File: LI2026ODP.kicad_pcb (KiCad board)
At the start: 4 copper layers, 18.8 x 39.9 mm, 34 parts, among them J1 9-1437539-2, J2 Conn_01x05_Male, U1 LM2936MM-3.3, U2 STM32G0B1KET6, U3 max6921aui

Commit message: Added SWCLK silk to PCB.
 Add SWCLK silk
 Issue : #6

 This was missing in the original design.
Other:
- board text added: "SWCLK"
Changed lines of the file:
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@@
   (general
     (thickness 1.6)
-    (drawings 12)
+    (drawings 13)
     (tracks 335)
     (zones 0)
@@
   (page A4)
   (layers
-    (0 F.Cu signal hide)
-    (1 In1.Cu power hide)
-    (2 In2.Cu signal hide)
-    (31 B.Cu signal hide)
+    (0 F.Cu signal)
+    (1 In1.Cu power)
+    (2 In2.Cu signal)
+    (31 B.Cu signal)
     (32 B.Adhes user hide)
     (33 F.Adhes user hide)
-    (34 B.Paste user hide)
+    (34 B.Paste user)
     (35 F.Paste user hide)
     (36 B.SilkS user)
-    (37 F.SilkS user hide)
+    (37 F.SilkS user)
     (38 B.Mask user)
-    (39 F.Mask user hide)
+    (39 F.Mask user)
     (40 Dwgs.User user hide)
     (41 Cmts.User user hide)
@@
       (net 76 /KEY0))
   )
+  (gr_text SWCLK (at 119.888 120.142) (layer F.SilkS)
+    (effects (font (size 0.6 0.5) (thickness 0.1)))
+  )
   (gr_text v1.0.0 (at 120.65 92.456 270) (layer F.SilkS)

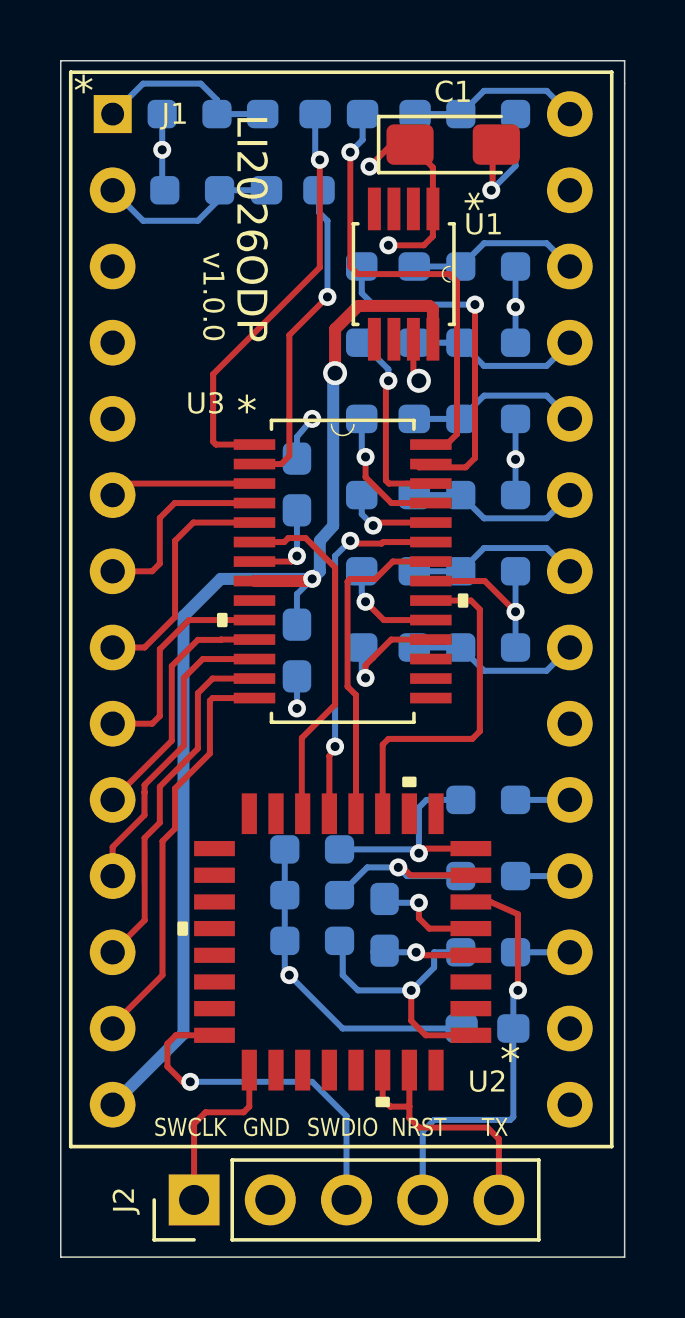
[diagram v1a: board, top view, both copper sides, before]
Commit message: Modify the U2 Footprint.
 Issue : #5

 The footprint was incorrect. Substitute it with the right 0.8mm pitch one.
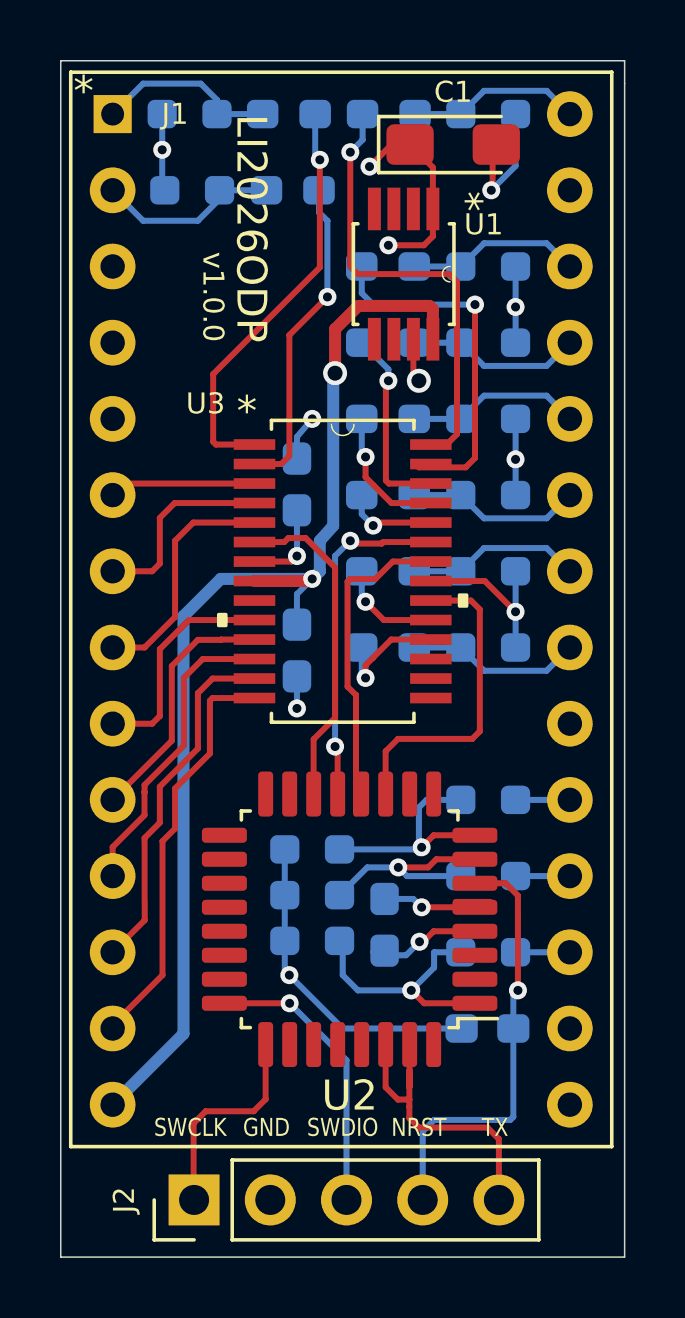
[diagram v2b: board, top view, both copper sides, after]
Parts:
- U2: footprint STM32G0B1:STM32G0B1KET6 -> Package_QFP:LQFP-32_7x7mm_P0.8mm
- moved U2 0.79 mm to (125.2, 113.2)
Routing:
- net /SWDIO: track 11.9 -> 9.34 mm
- net /LPUART2_TX: track 8.86 -> 10.7 mm
- net /SWCLK: track 6.47 -> 7.59 mm
- net /MOSI: track 12.6 -> 11.5 mm
- net /KEY0: track 9.21 -> 8.31 mm
- net /BLANK: track 11.5 -> 10.7 mm
- net GND: track 36.6 -> 37.3 mm
- net /LOAD: track 12.1 -> 11.4 mm
- net /KEY2: track 7.01 -> 7.67 mm

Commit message: Add capacitor for 25v line
 Issue #8 .

 Add C6 close to the voltage regulator.
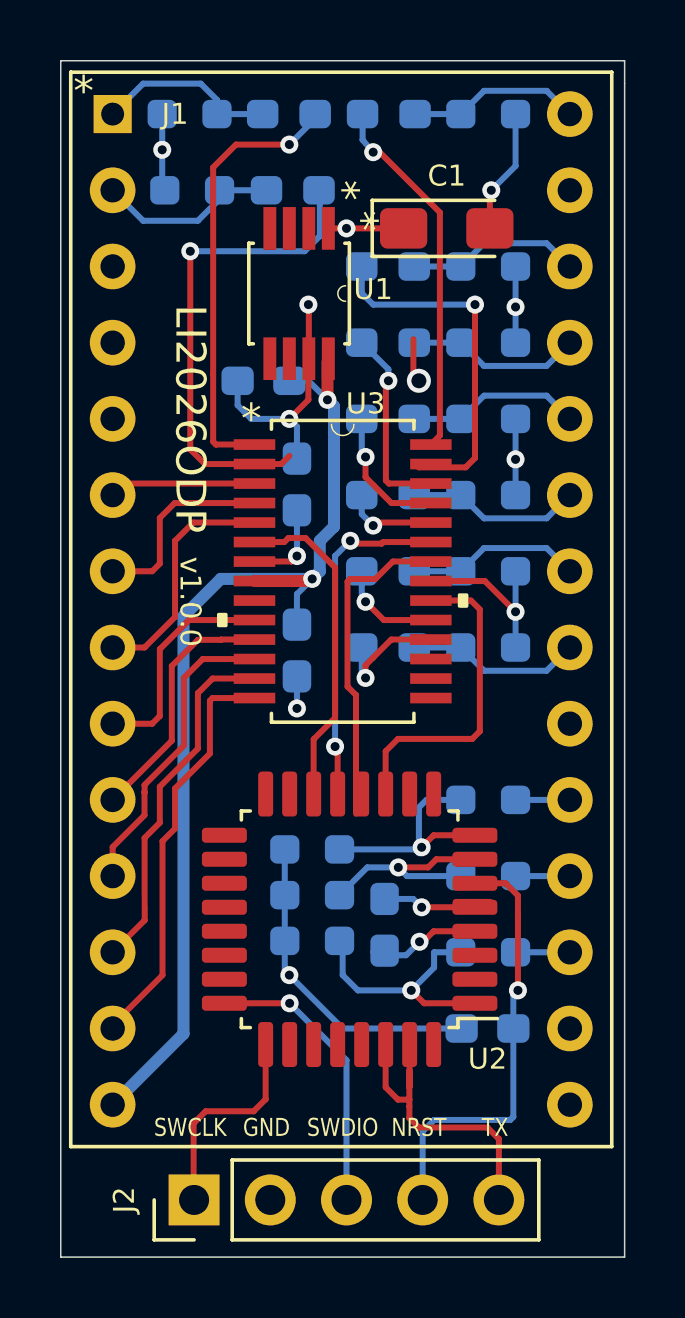
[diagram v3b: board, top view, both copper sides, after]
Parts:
- added C6: 0.1u, Capacitor_SMD:C_0603_1608Metric_Pad1.08x0.95mm_HandSolder, B.Cu at (122.3, 95.2)
- moved U1 3.54 mm to (123.5, 92.3)
- moved C1 2.80 mm to (128.4, 90.2)
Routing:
- net GND: track 37.3 -> 43.9 mm, vias 10 -> 11
- net /D0: track 11.8 -> 17.3 mm
- net +3V3: track 13.9 -> 9.77 mm, vias 4 -> 3
- net /+25V: track 39.1 -> 35.0 mm
- net /D2: track 15.6 -> 12.3 mm
- net /D1: track 14.9 -> 15.6 mm

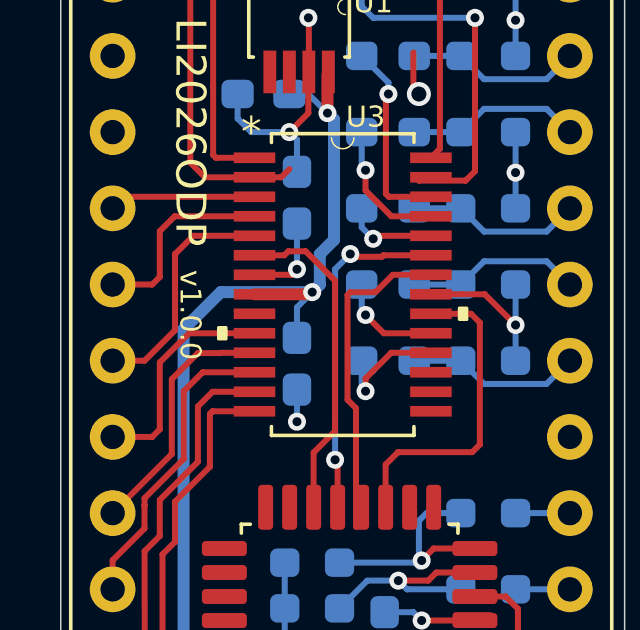
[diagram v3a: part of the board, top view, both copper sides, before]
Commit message: Version number should be updated.
 Issue : #9

 Update silk of PCB  from 1.0.0 to 1.0.1
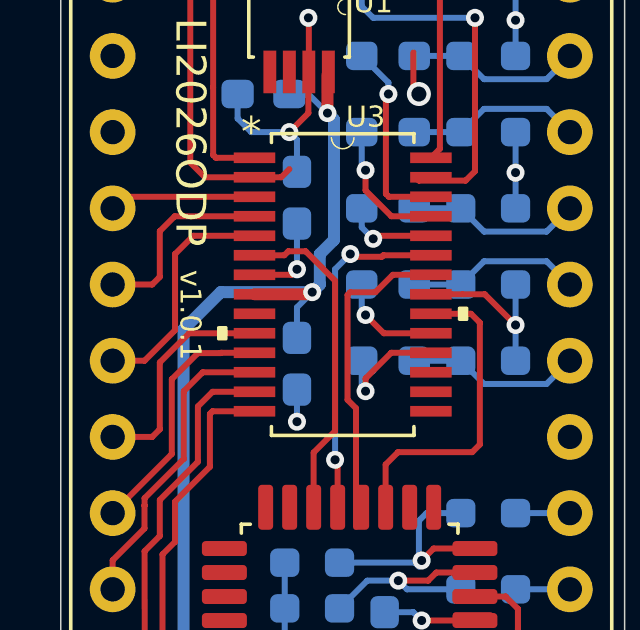
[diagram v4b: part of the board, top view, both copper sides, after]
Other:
- board text added: "v1.0.1"
- board text removed: "v1.0.0"
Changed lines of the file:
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@@
     (effects (font (size 0.6 0.5) (thickness 0.1)))
   )
-  (gr_text v1.0.0 (at 119.888 102.616 270) (layer F.SilkS)
+  (gr_text v1.0.1 (at 119.888 102.616 -90) (layer F.SilkS)
     (effects (font (size 0.7 0.7) (thickness 0.1)))
   )
